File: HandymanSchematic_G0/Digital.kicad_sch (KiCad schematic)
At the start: 13 parts, among them J301 SWI, SW301 RST, U301 STM32G030F6P6, U302 AMS1117

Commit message: prelim pinout
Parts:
- removed R301, R302: 2k2, PCM_Resistor_SMD_AKL:R_0805_2012Metric, symbol Device:R_US
- added C8, C9: 6p, Capacitor_SMD:C_0805_2012Metric, symbol Device:C
- added R15: 47k, PCM_Resistor_SMD_AKL:R_0805_2012Metric, symbol Device:R_US
- added Y1: 32.768kHZ, Crystal:Crystal_SMD_SeikoEpson_MC306-4Pin_8.0x3.2mm, symbol Device:Crystal_GND23
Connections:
- net +3.3V: now also R15.1
- net GND: now also C8.2, C9.2, Y1.2, Y1.3
- net TUNE_IN: now reaches U301.10 (PA3)
- net OPEN_OUT: now reaches U301.11 (PA4)
- net at U301.2 (PC14/PB9): now also C9.1, Y1.1
- net at U301.3 (PC15): now also C8.1, Y1.4
- net TunerModeIn: now reaches U301.8 (PA1)
- net TunerModeIn: now also R15.2
- net OPEN_IN: now reaches U301.9 (PA2)
- no-connect marks 11 -> 5
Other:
- note added: "GPIOs to assign: - Tuning in (interrupt) - Gate Open in (interrupt) - Gate bypass in - Tuner mode in - Gate Open out - Gate mode on LED out"
- moved on the sheet: C301, C302, C303, C304, C305, C306, J301, R303, SW301, U301, U302

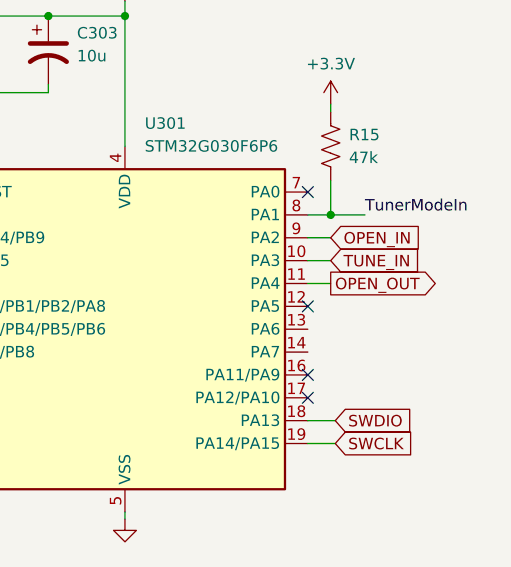
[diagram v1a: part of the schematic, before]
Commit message: attenuator input change
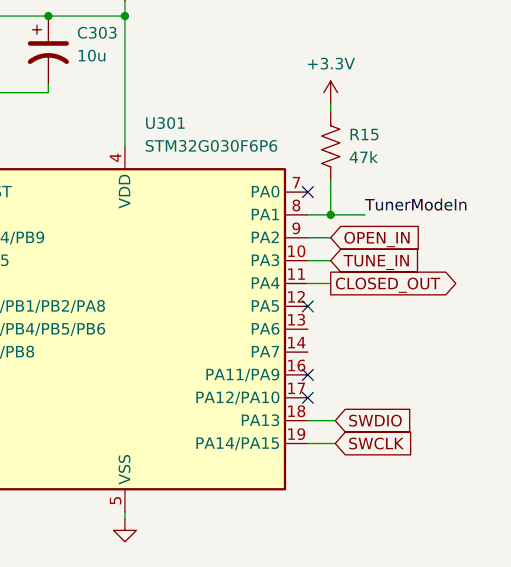
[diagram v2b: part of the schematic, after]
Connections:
- net OPEN_OUT renamed CLOSED_OUT
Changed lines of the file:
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@@
 		)
 	)
-	(global_label "OPEN_OUT"
+	(global_label "CLOSED_OUT"
 		(shape output)
 		(at 179.07 67.31 0)

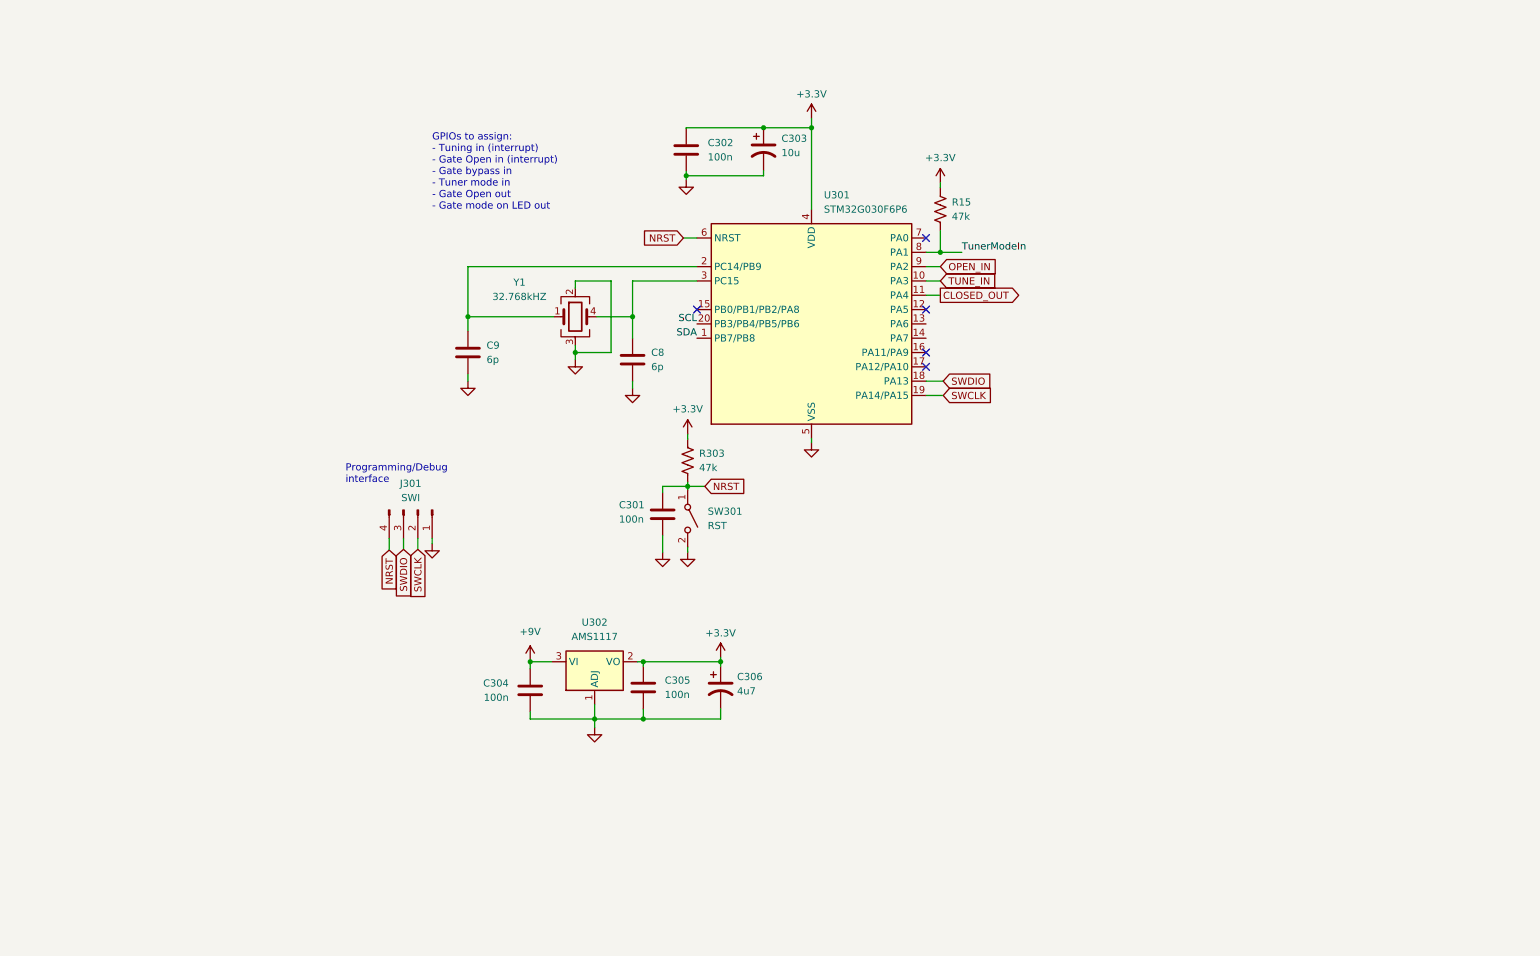
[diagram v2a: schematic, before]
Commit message: digital side schematic
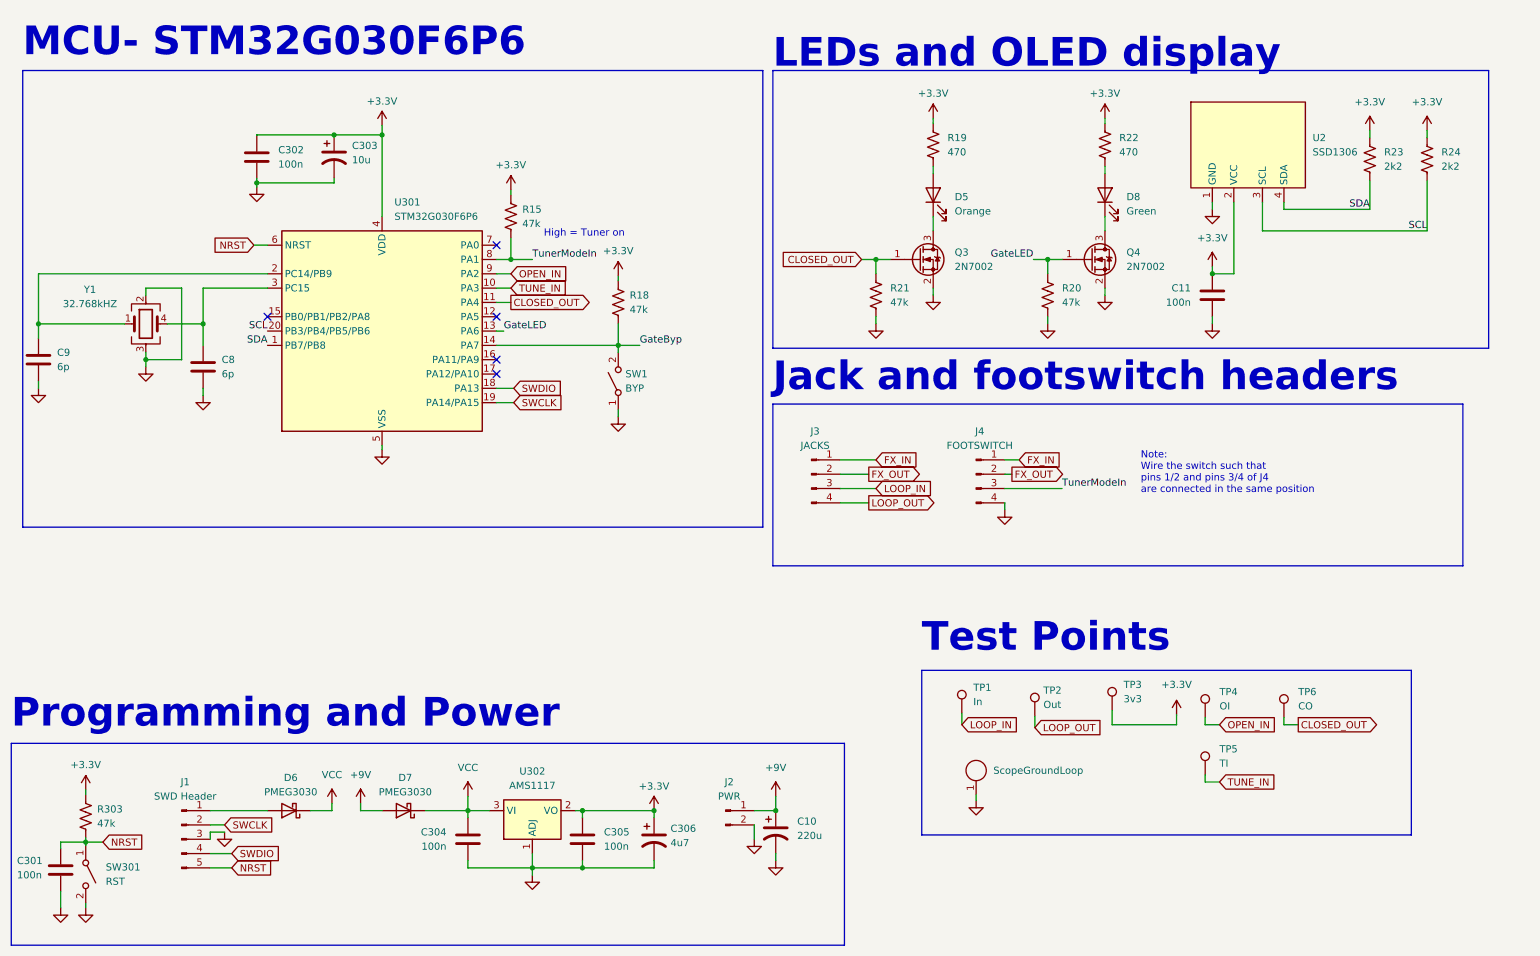
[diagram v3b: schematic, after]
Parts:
- removed J301: SWI, Connector_PinHeader_2.54mm:PinHeader_1x04_P2.54mm_Vertical, symbol Connector:Conn_01x04_Pin
- added C10: 220u, Capacitor_THT:CP_Radial_D5.0mm_P2.50mm, symbol Device:C_Polarized_US
- added C11: 100n, Capacitor_SMD:C_0805_2012Metric, symbol Device:C
- added D5: Orange, LED_THT:LED_D3.0mm, symbol Device:LED
- added D6, D7: PMEG3030, Diode_SMD:D_SOD-123, symbol Device:D_Schottky
- added D8: Green, LED_THT:LED_D3.0mm, symbol Device:LED
- added J1: SWD Header, Connector_PinHeader_2.54mm:PinHeader_1x05_P2.54mm_Vertical, symbol Connector:Conn_01x05_Pin
- added J2: PWR, Connector_PinHeader_2.54mm:PinHeader_1x02_P2.54mm_Vertical, symbol Connector:Conn_01x02_Pin
- added J3: JACKS, Connector_PinHeader_2.54mm:PinHeader_1x04_P2.54mm_Vertical, symbol Connector:Conn_01x04_Pin
- added J4: FOOTSWITCH, Connector_PinHeader_2.54mm:PinHeader_1x04_P2.54mm_Vertical, symbol Connector:Conn_01x04_Pin
- added J5: ScopeGroundLoop, Connector:THT_GND_WIRE, symbol Connector:ScopeGroundLoop
- added Q3, Q4: 2N7002, Package_TO_SOT_SMD:SOT-23, symbol Transistor_FET:2N7002
- added R18: 47k, PCM_Resistor_SMD_AKL:R_0805_2012Metric, symbol Device:R_US
- added R19, R22: 470, PCM_Resistor_SMD_AKL:R_0805_2012Metric, symbol Device:R_US
- added R20, R21: 47k, symbol Device:R_US
- added R23, R24: 2k2, symbol Device:R_US
- added SW1: BYP, symbol Switch:SW_SPST
- added TP1: In, TestPoint:TestPoint_THTPad_D2.0mm_Drill1.0mm_VAL, symbol Connector:TestPoint
- added TP2: Out, TestPoint:TestPoint_THTPad_D2.0mm_Drill1.0mm_VAL, symbol Connector:TestPoint
- added TP3: 3v3, TestPoint:TestPoint_THTPad_D2.0mm_Drill1.0mm_VAL, symbol Connector:TestPoint
- added TP4: OI, TestPoint:TestPoint_THTPad_D2.0mm_Drill1.0mm_VAL, symbol Connector:TestPoint
- added TP5: TI, TestPoint:TestPoint_THTPad_D2.0mm_Drill1.0mm_VAL, symbol Connector:TestPoint
- added TP6: CO, TestPoint:TestPoint_THTPad_D2.0mm_Drill1.0mm_VAL, symbol Connector:TestPoint
- added U2: SSD1306, Display:SSD1306_OLED_128x64, symbol Display_Graphic:SSD1306_OLED_128x64
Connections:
- net +3.3V: now also C11.2, R18.1, R19.1, R22.1, R23.1, R24.1, TP3.1, U2.2 (VCC)
- net +9V: now also C10.1, D7.2 (A), J2.1 (Pin_1); no longer C304.2, U302.3 (VI)
- net CLOSED_OUT: now also Q3.1 (G), R21.2, TP6.1
- net GND: now also C10.2, C11.1, J1.3 (Pin_3), J2.2 (Pin_2), J4.4 (Pin_4), J5.1, Q3.2 (S), Q4.2 (S), R20.1, R21.1, SW1.1 (A), U2.1 (GND)
- net NRST: now also J1.5 (Pin_5)
- net OPEN_IN: now also TP4.1
- net SCL: now also R24.2, U2.3 (SCL)
- net SDA: now also R23.2, U2.4 (SDA)
- net SWCLK: now also J1.2 (Pin_2)
- net SWDIO: now also J1.4 (Pin_4)
- net TUNE_IN: now also TP5.1
- net TunerModeIn: now also J4.3 (Pin_3)
- net GateLED: now reaches U301.13 (PA6)
- net GateLED: now also Q4.1 (G), R20.2
- net GateByp: now reaches U301.14 (PA7)
- net GateByp: now also R18.2, SW1.2 (B)
- new net: D5.1 (K), Q3.3 (D)
- new net: D6.2 (A), J1.1 (Pin_1)
- new net: D5.2 (A), R19.2
- new net: D8.2 (A), R22.2
- new net: D8.1 (K), Q4.3 (D)
- new net FX_IN: J3.1 (Pin_1), J4.1 (Pin_1)
- new net FX_OUT: J3.2 (Pin_2), J4.2 (Pin_2)
- new net LOOP_IN: J3.3 (Pin_3), TP1.1
- new net LOOP_OUT: J3.4 (Pin_4), TP2.1
- new net VCC: C304.2, D6.1 (K), D7.1 (K), U302.3 (VI)
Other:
- note added: "High = Tuner on"
- note added: "Jack and footswitch headers"
- note added: "LEDs and OLED display"
- note added: "MCU- STM32G030F6P6"
- note added: "Note: Wire the switch such that pins 1/2 and pins 3/4 of J4 are connected in the same position"
- note added: "Programming and Power"
- note added: "Test Points"
- note removed: "GPIOs to assign: - Tuning in (interrupt) - Gate Open in (interrupt) - Gate bypass in - Tuner mode in - Gate Open out - Gate mode on LED out"
- note removed: "Programming/Debug interface"
- moved on the sheet: C301, C302, C303, C304, C305, C306, C8, C9, R15, R303, SW301, U301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

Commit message: footprints chosen, test points
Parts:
- R15, R18, R19, R22, R303: footprint PCM_Resistor_SMD_AKL:R_0805_2012Metric -> Resistor_SMD:R_0805_2012Metric
- R20, R21, R23, R24, SW1: footprint (none) -> Resistor_SMD:R_0805_2012Metric
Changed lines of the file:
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@@
 	(label "SCL"
 		(at 265.43 55.88 180)
+		(fields_autoplaced yes)
 		(effects
 			(font
@@
 	(label "SCL"
 		(at 59.69 73.66 180)
+		(fields_autoplaced yes)
 		(effects
 			(font
@@
 	(label "TunerModeIn"
 		(at 106.68 60.96 0)
+		(fields_autoplaced yes)
 		(effects
 			(font
@@
 	(label "GateByp"
 		(at 125.73 76.2 0)
+		(fields_autoplaced yes)
 		(effects
 			(font
@@
 	(label "SDA"
 		(at 59.69 76.2 180)
+		(fields_autoplaced yes)
 		(effects
 			(font
@@
 	(label "SDA"
 		(at 255.27 52.07 180)
+		(fields_autoplaced yes)
 		(effects
 			(font
@@
 	(label "GateLED"
 		(at 101.6 73.66 0)
+		(fields_autoplaced yes)
 		(effects
 			(font
@@
 	(label "TunerModeIn"
 		(at 200.66 101.6 0)
+		(fields_autoplaced yes)
 		(effects
 			(font
@@
 	(label "GateLED"
 		(at 195.58 60.96 180)
+		(fields_autoplaced yes)
 		(effects
 			(font
@@
 			)
 		)
-		(property "Footprint" "PCM_Resistor_SMD_AKL:R_0805_2012Metric"
+		(property "Footprint" "Resistor_SMD:R_0805_2012Metric"
 			(at 28.448 160.02 90)
 			(effects
@@
 			)
 		)
-		(property "Footprint" ""
+		(property "Footprint" "Resistor_SMD:R_0805_2012Metric"
 			(at 166.624 67.056 90)
 			(effects
@@
 			)
 		)
-		(property "Footprint" "PCM_Resistor_SMD_AKL:R_0805_2012Metric"
+		(property "Footprint" "Resistor_SMD:R_0805_2012Metric"
 			(at 178.816 40.894 90)
 			(effects
@@
 			)
 		)
-		(property "Footprint" ""
+		(property "Footprint" "Resistor_SMD:R_0805_2012Metric"
 			(at 121.92 82.55 0)
 			(effects
@@
 			)
 		)
-		(property "Footprint" "PCM_Resistor_SMD_AKL:R_0805_2012Metric"
+		(property "Footprint" "Resistor_SMD:R_0805_2012Metric"
 			(at 209.296 40.894 90)
 			(effects
@@
 			)
 		)
-		(property "Footprint" "PCM_Resistor_SMD_AKL:R_0805_2012Metric"
+		(property "Footprint" "Resistor_SMD:R_0805_2012Metric"
 			(at 122.936 68.834 90)
 			(effects
@@
 			)
 		)
-		(property "Footprint" ""
+		(property "Footprint" "Resistor_SMD:R_0805_2012Metric"
 			(at 256.286 43.434 90)
 			(effects
@@
 			)
 		)
-		(property "Footprint" "PCM_Resistor_SMD_AKL:R_0805_2012Metric"
+		(property "Footprint" "Resistor_SMD:R_0805_2012Metric"
 			(at 103.886 53.594 90)
 			(effects
@@
 			)
 		)
-		(property "Footprint" ""
+		(property "Footprint" "Resistor_SMD:R_0805_2012Metric"
 			(at 266.446 43.434 90)
 			(effects
@@
 			)
 		)
-		(property "Footprint" ""
+		(property "Footprint" "Resistor_SMD:R_0805_2012Metric"
 			(at 197.104 67.056 90)
 			(effects

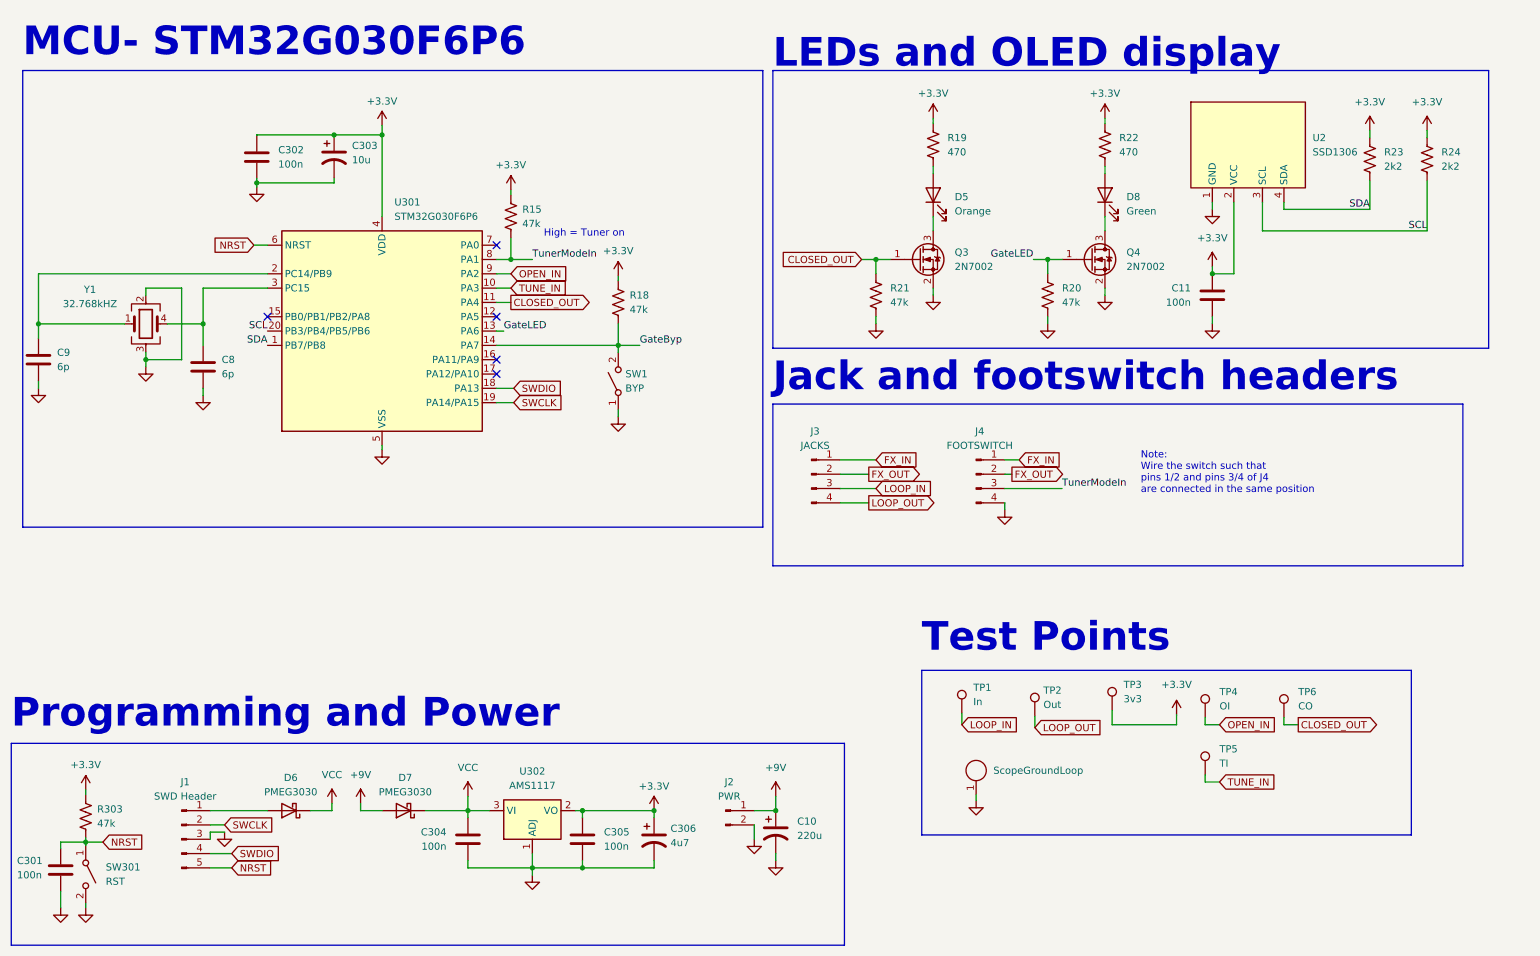
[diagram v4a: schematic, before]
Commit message: footprints, enclosure areas drawn
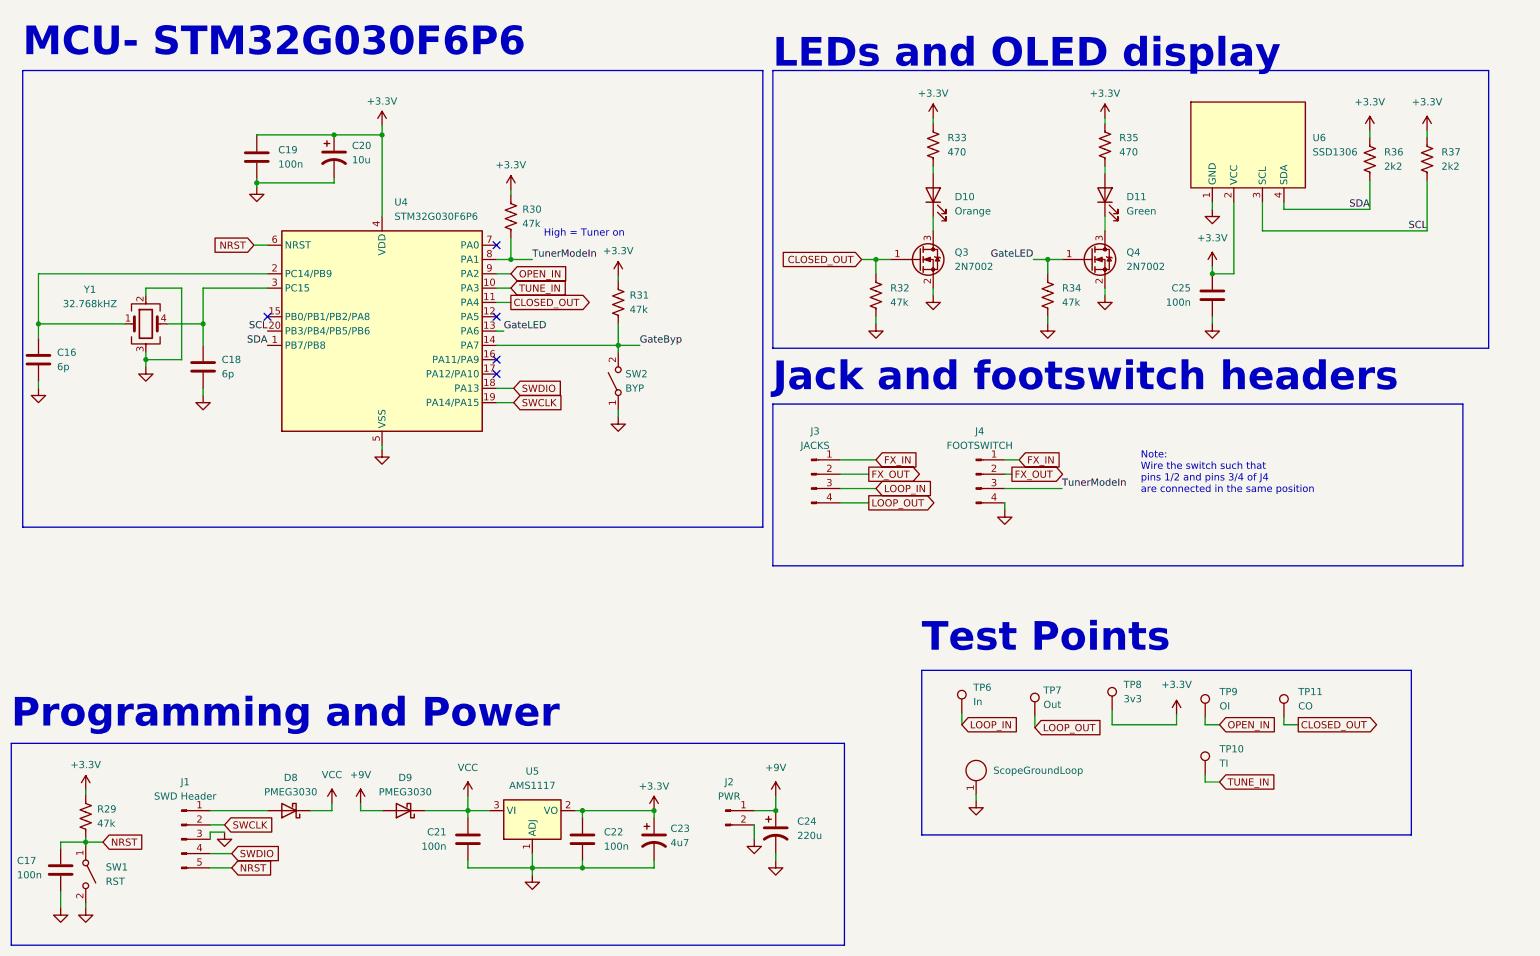
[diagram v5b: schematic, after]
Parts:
- SW2: renamed from SW1; footprint Resistor_SMD:R_0805_2012Metric -> Button_Switch_THT:MiniToggle_SPST
- renumbered C9 to C16, C301 to C17, C8 to C18, C302 to C19, C303 to C20, C304 to C21, C305 to C22, C306 to C23, C10 to C24, C11 to C25, D5 to D10, D8 to D11, D6 to D8, D7 to D9, R303 to R29, R15 to R30, R18 to R31, R21 to R32, R19 to R33, R20 to R34, R22 to R35, R23 to R36, R24 to R37, SW301 to SW1, TP5 to TP10, TP6 to TP11, TP1 to TP6, TP2 to TP7, TP3 to TP8, TP4 to TP9, U301 to U4, U302 to U5, U2 to U6
